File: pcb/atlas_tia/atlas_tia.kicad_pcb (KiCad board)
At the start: 2 copper layers, 18 parts, among them J1 TIA_LINK, J2 TIP_CONTACT, J3 SHIELD_CONTACT, U1 OPA828IDR

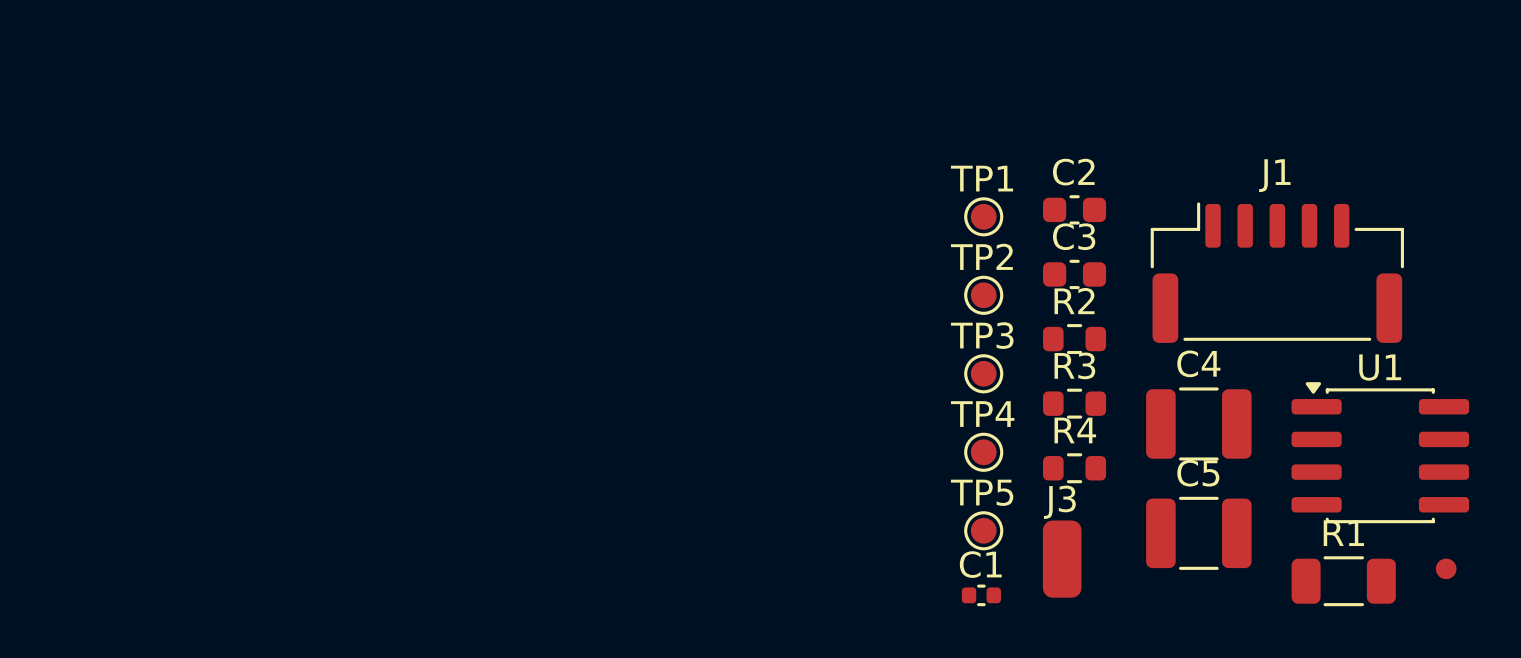
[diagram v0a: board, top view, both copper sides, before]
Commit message: TIA layout updates, guard footprints and LTspice compensation study
- Update TIA schematic, board and project
- Add guard-ring variants of C_0603, R_1206 and SOIC-8 footprints to atlas_parts_lib
- Add LTspice TIA netlists (proxy and TI OPAx828 model), analysis scripts and sweep results

Co-Authored-By: Claude Opus 5.5 <noreply@anthropic.com>
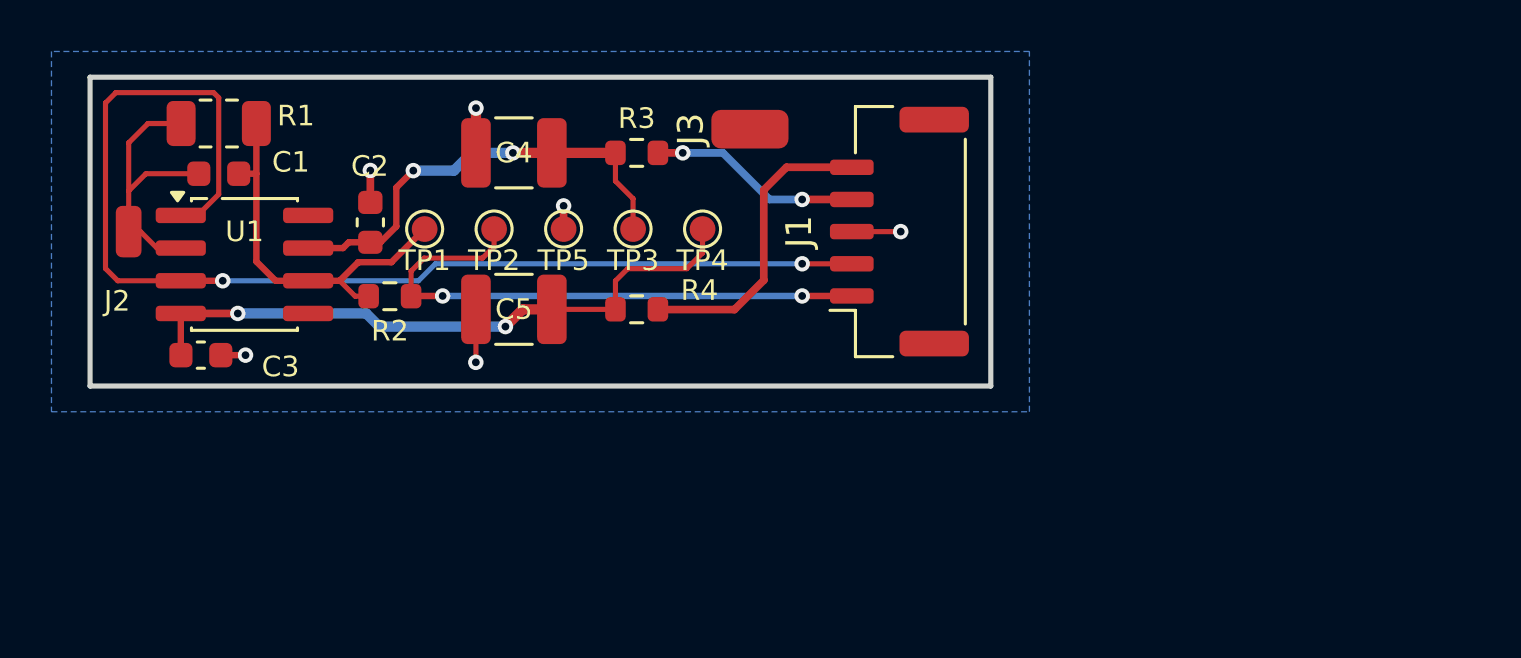
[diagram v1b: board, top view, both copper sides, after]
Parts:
- C1: value 0.5pF -> 0.2pF; footprint Capacitor_SMD:C_0402_1005Metric -> atlas_parts_lib:C_0603_1608Metric_Guard
- J2: footprint atlas_parts_lib:TipContact_Pad_D0.8mm -> Connector_Wire:SolderWirePad_1x01_SMD_1x2mm
- R1: footprint Resistor_SMD:R_1206_3216Metric -> atlas_parts_lib:R_1206_3216Metric_Guard
- U1: footprint Package_SO:SOIC-8_3.9x4.9mm_P1.27mm -> atlas_parts_lib:SOIC-8_3.9x4.9mm_P1.27mm_Guard
- moved J2 52.8 mm to (84.0, 95.0)
- moved R1 47.2 mm to (87.5, 90.8)
- moved U1 44.8 mm to (88.5, 96.3)
- moved C3 34.1 mm to (86.8, 99.8)
- moved C1 33.9 mm to (87.5, 92.8)
- moved C4 28.6 mm to (99.0, 91.9), turned to 180 degrees
- moved C5 28.0 mm to (99.0, 98.0), turned to 180 degrees
- moved C2 27.4 mm to (93.4, 94.6), turned to 90 degrees
- moved R2 26.7 mm to (94.2, 97.5)
- moved TP1 21.7 mm to (95.5, 94.9)
- moved J3 20.6 mm to (108.1, 91.0), turned to 90 degrees
- moved TP5 20.1 mm to (100.9, 94.9)
- moved R3 19.6 mm to (103.7, 91.9), turned to 180 degrees
- moved TP2 19.2 mm to (98.2, 94.9)
- moved R4 18.1 mm to (103.7, 98.0), turned to 180 degrees
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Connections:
- U1 pad 1: unconnected-(U1-NC-Pad1) -> GNDA
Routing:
- net GNDA: track 0.00 -> 35.2 mm, vias 0 -> 8
- net VEE_TIA: track 0.00 -> 24.9 mm, vias 0 -> 2
- net TIA_OUT: track 0.00 -> 22.4 mm, vias 0 -> 2
- net VCC_TIA: track 0.00 -> 17.6 mm, vias 0 -> 2
- net TIA_RAW: track 0.00 -> 15.1 mm
- net -15V: track 0.00 -> 11.9 mm
- net TIP_IN: track 0.00 -> 11.1 mm
- net +15V: track 0.00 -> 8.28 mm, vias 0 -> 2
- added copper zone on B.Cu, net GNDA
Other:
- board outline added: 35 x 12 mm
